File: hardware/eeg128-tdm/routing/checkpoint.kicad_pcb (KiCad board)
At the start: 4 copper layers, 190 x 110 mm, 642 parts, among them J1 J1, J10 J10, J11 J11, J2 J2, J3 J3, J4 J4, J5 J5, J6 J6, J7 J7, J8 J8, J9 TYPE-C-31-M-12, U1 U1, U10 U10, U11 U11, U12 U12, U13 U13, U14 U14, U15 U15, U16 U16, U17 U17, U18 U18, U19 U19, U2 U2, U20 U20, U21 U21, U22 U22, U23 U23, U24 U24, U25 U25, U26 U26, U27 U27, U3 U3, U4 U4, U5 U5, U6 U6, U7 U7, U8 U8, U9 U9, Y1 Y1

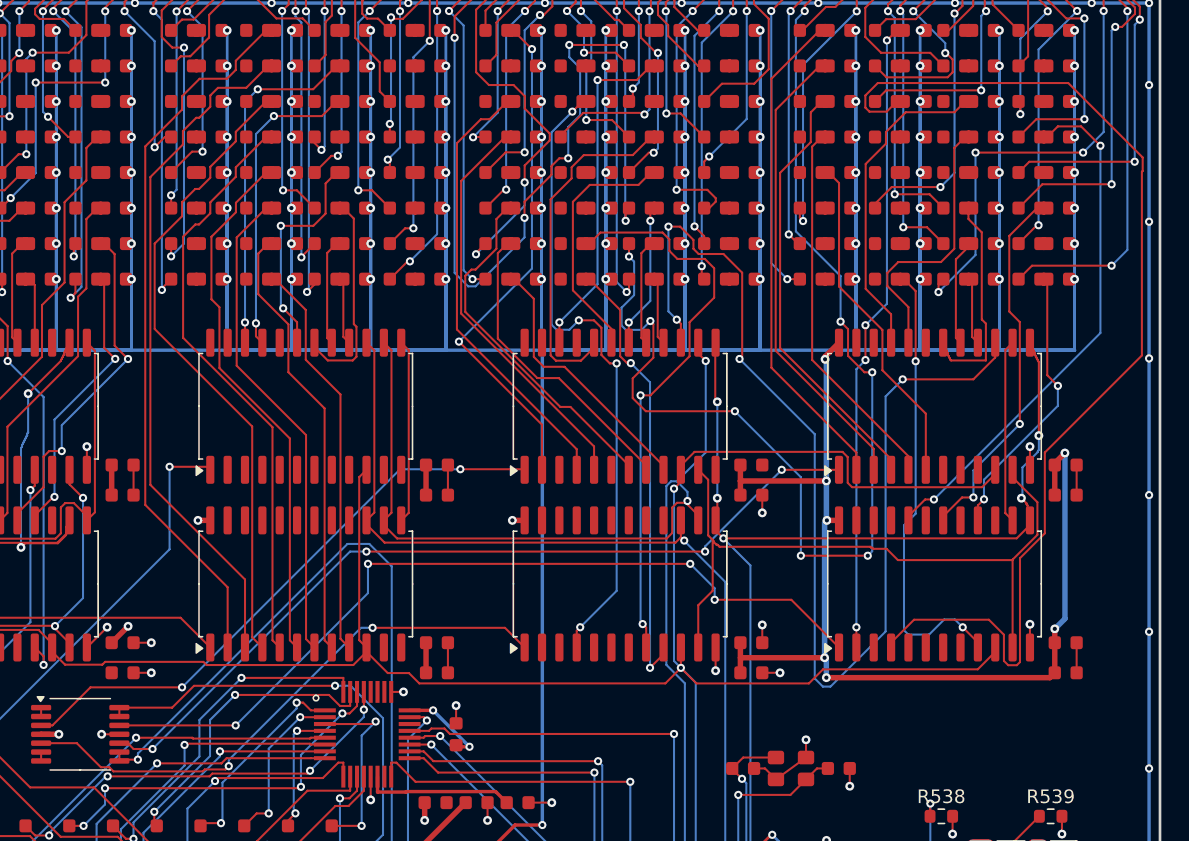
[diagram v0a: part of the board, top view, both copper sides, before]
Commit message: Continue validated A2 checkpoint at 308 native opens
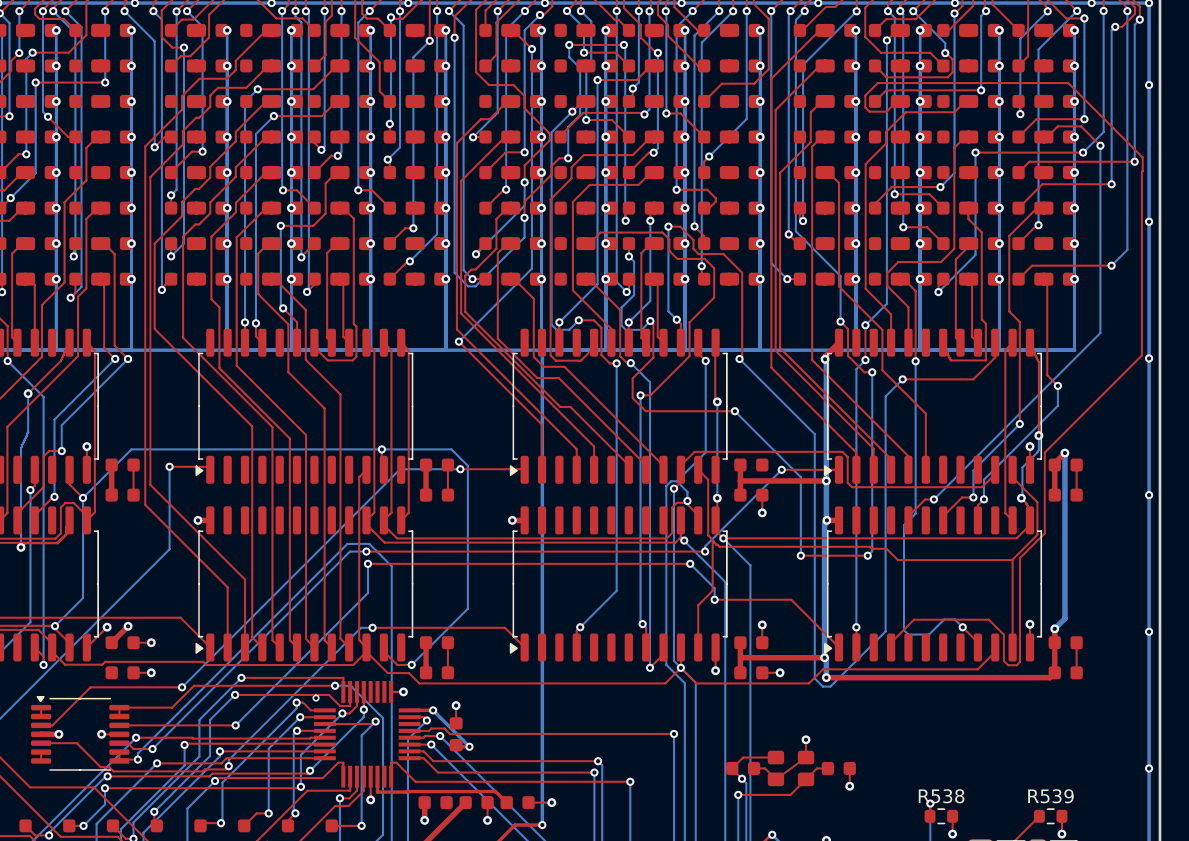
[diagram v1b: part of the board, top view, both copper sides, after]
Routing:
- net MUX_S1: track 235.9 -> 286.6 mm, vias 9 -> 11
